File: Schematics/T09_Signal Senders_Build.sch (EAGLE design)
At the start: 27 parts, among them IC1 7805TV, IC2 ATMEGA328, SW1 , Y2 16MHz

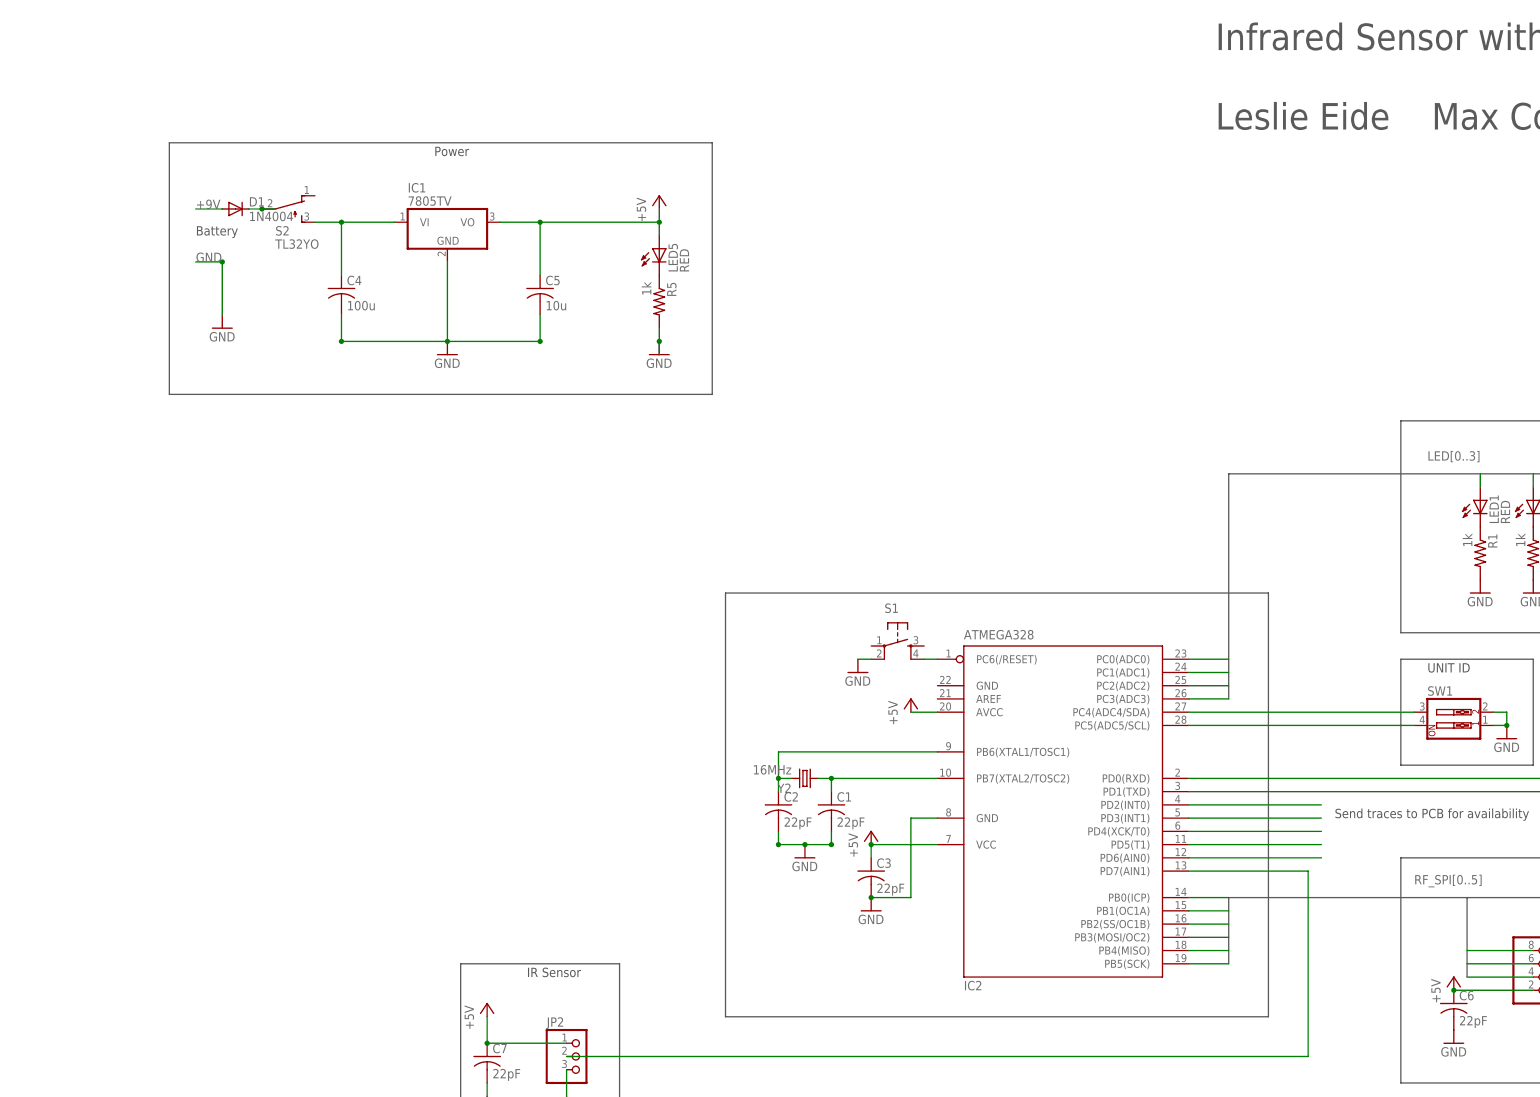
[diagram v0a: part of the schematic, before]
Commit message: Added 3.3V Rail. Can use panel mounted DC barrel.
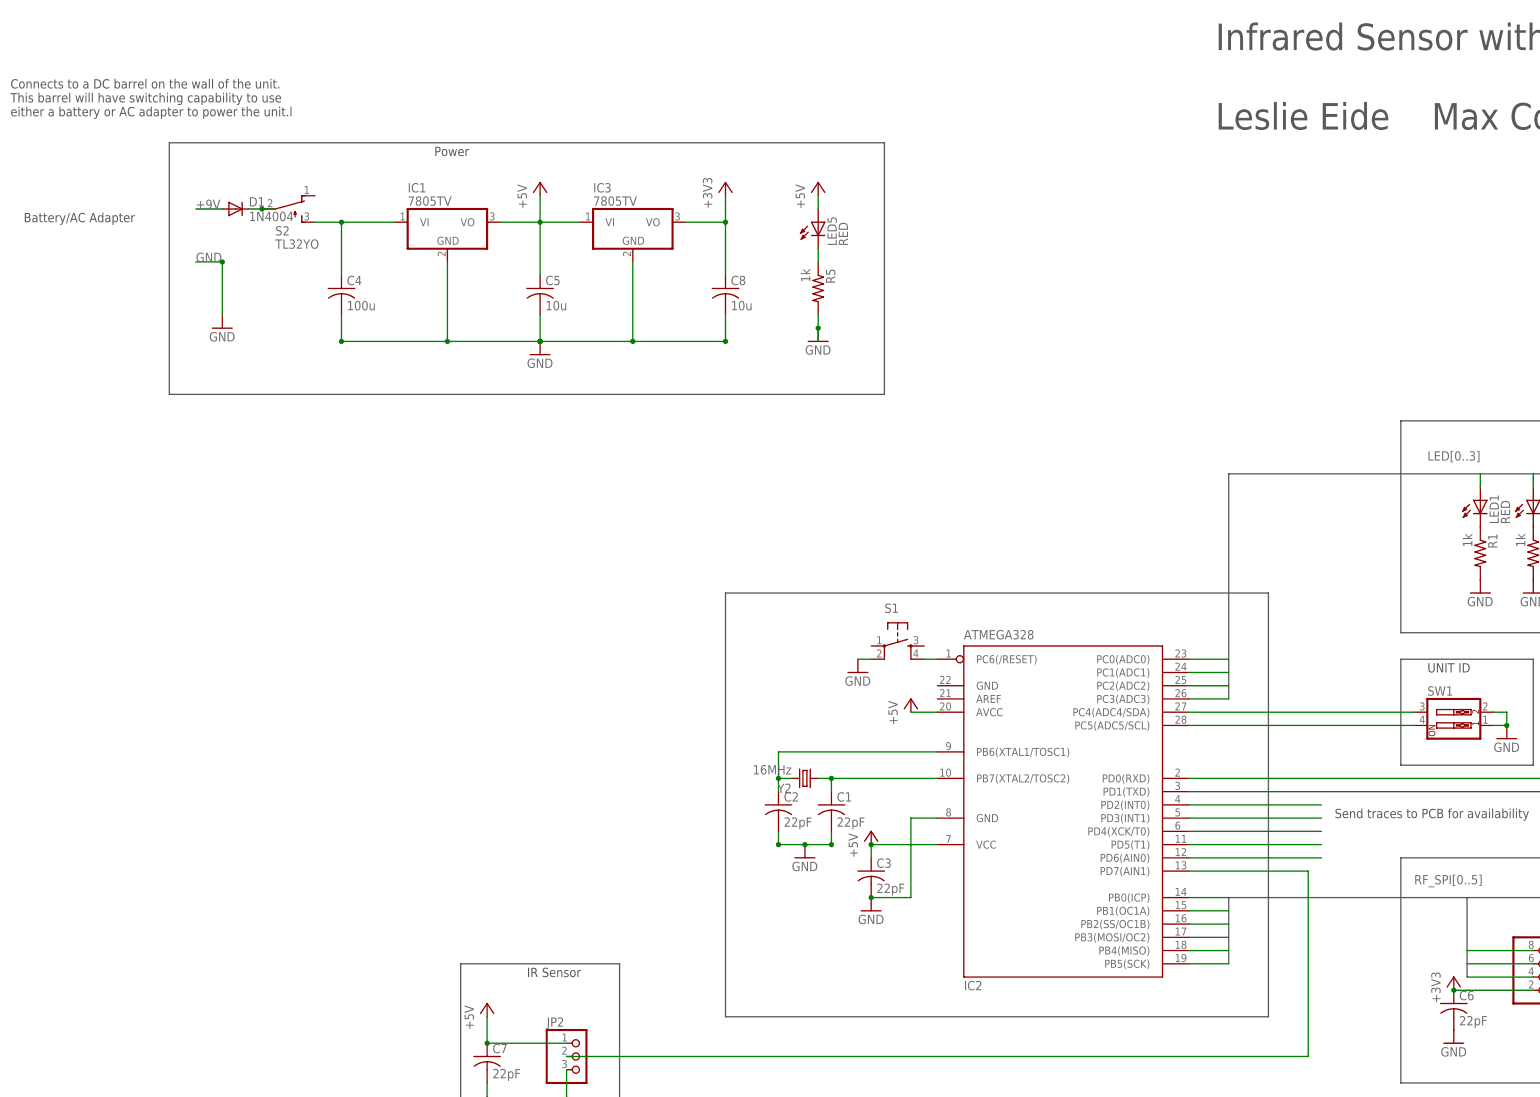
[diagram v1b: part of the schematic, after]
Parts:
- added C8: 10u, rcl:C-US025-025X050
- added IC3: 7805TV, linear:7805TV
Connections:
- new net +3V3: C6.1, C8.1, IC3.VO, JP1.2
- net +5V: now also IC3.VI; no longer C6.1, JP1.2
- net GND: now also C8.2, IC3.GND
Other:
- note added: "Battery/AC Adapter"
- note added: "Connects to a DC barrel on the wall of the unit. This barrel will have switching capability to use either a battery or AC adapter to power the unit.l"
- note removed: "Battery"
- moved on the sheet: LED5, R5

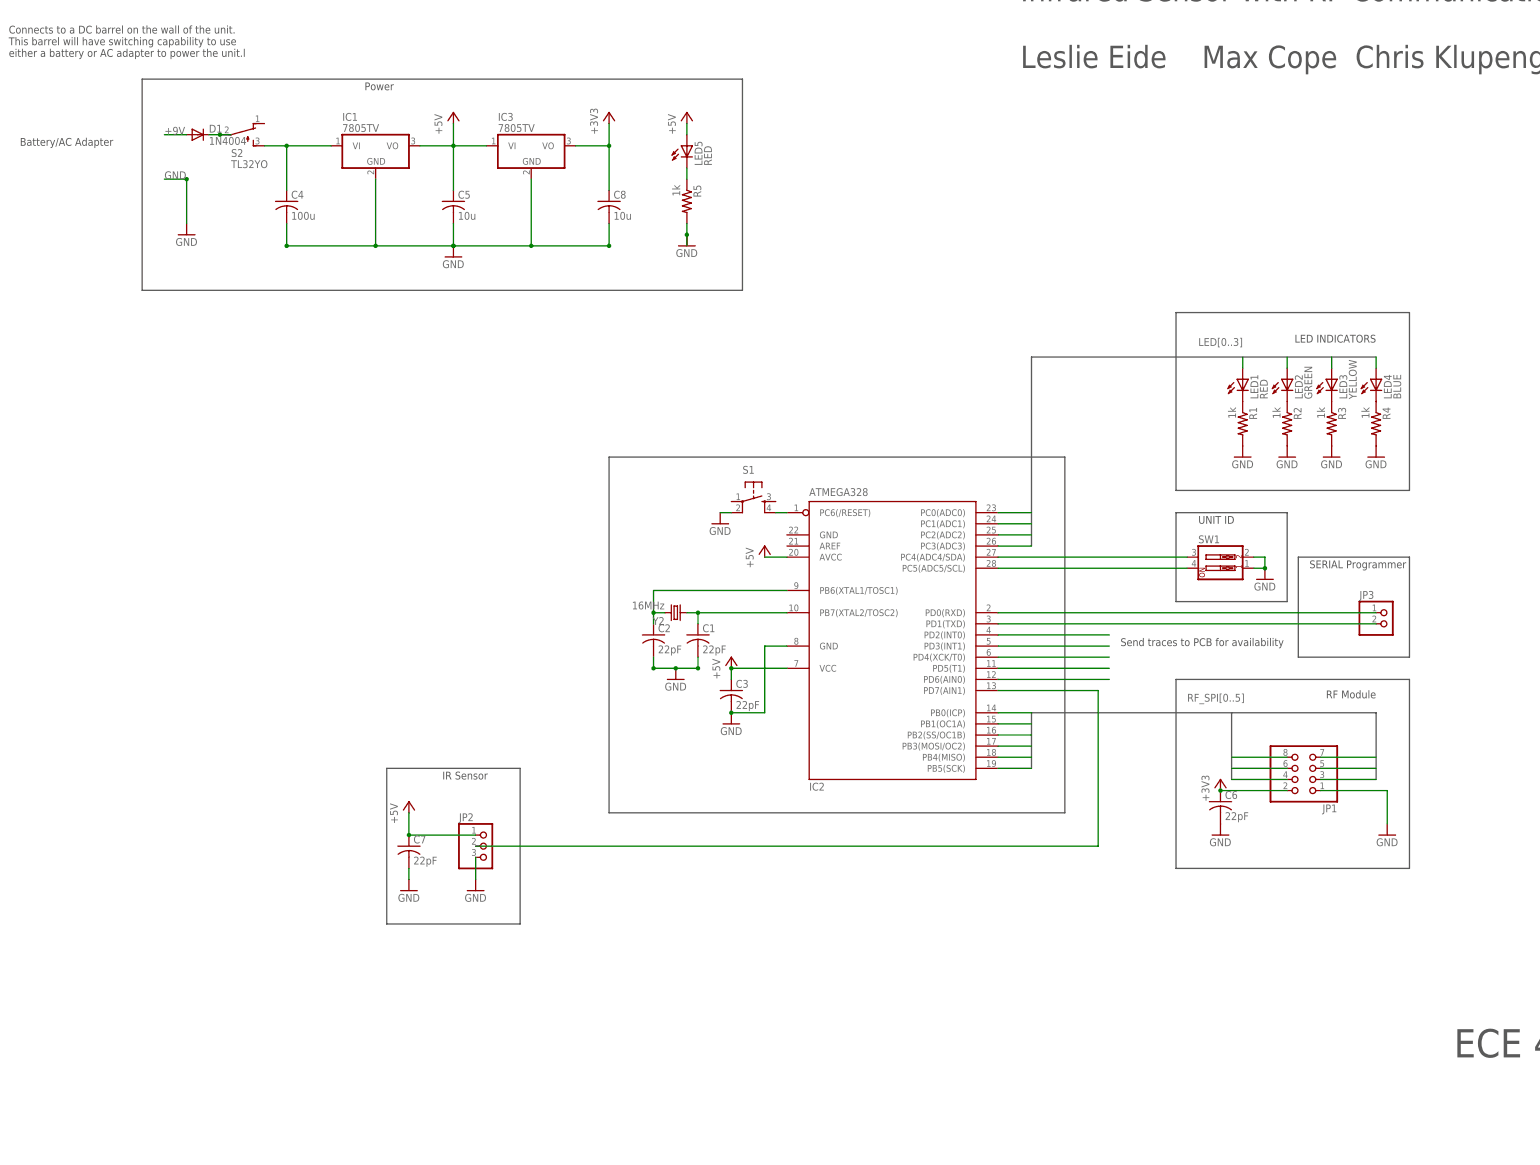
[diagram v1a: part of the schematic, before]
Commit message: Modified SPI section. Added DC barrel.
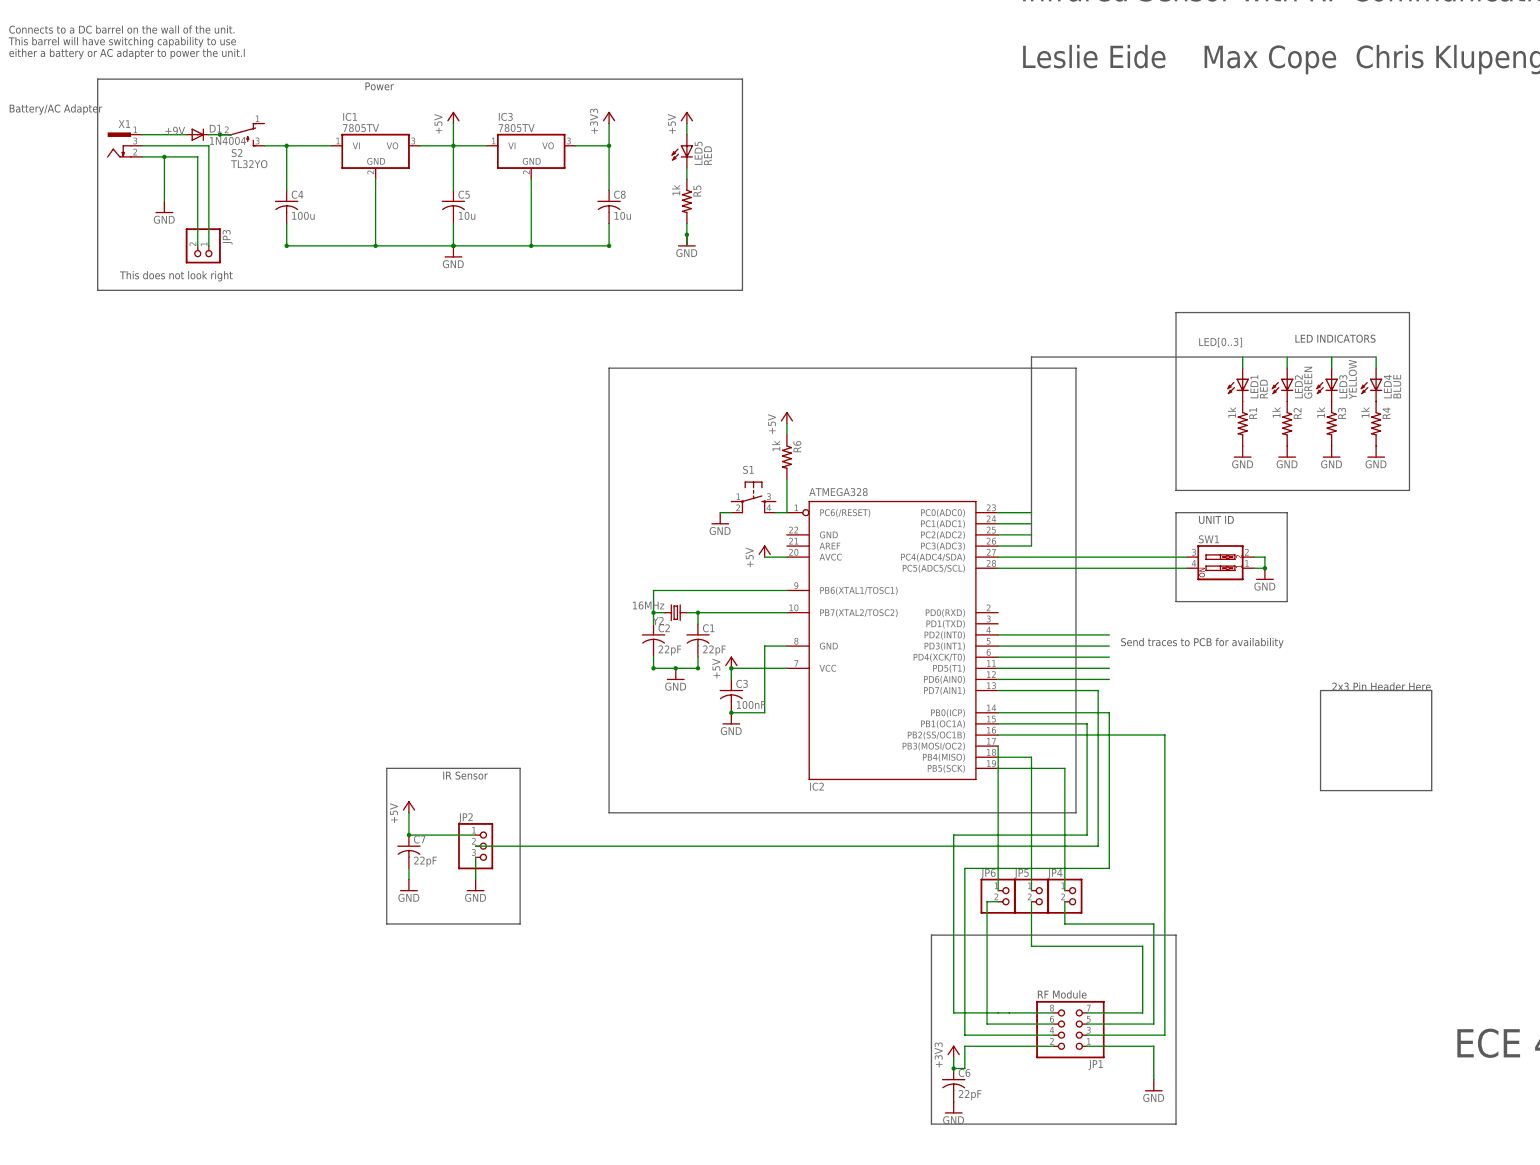
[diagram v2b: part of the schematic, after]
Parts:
- added JP4, JP5, JP6: (no value), pinhead:PINHD-1X2/90
- added R6: 1k, rcl:R-US_M0805
- added X1: (no value), con-conrad:733980-62
- C3: value 22pF -> 100nF
- JP3: value (none) -> (none); device pinhead:PINHD-1X2 -> pinhead:PINHD-1X2/90
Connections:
- removed net N$14: IC2.PD1(TXD), JP3.2
- net +5V: now also R6.1
- net +9V: now also X1.1
- net N$1: now also R6.2
- net N$13: now also X1.3; no longer IC2.PD0(RXD), JP3.1
- net RF_SPI0: now also IC2.PB2(SS/OC1B), JP1.4
- net RF_SPI1: now also JP1.8; no longer JP1.4
- net RF_SPI2: now also JP4.2; no longer IC2.PB2(SS/OC1B)
- net RF_SPI3: now also JP6.1, JP6.2
- net RF_SPI4: now also JP5.1, JP5.2
- net RF_SPI5: now also JP4.1; no longer JP1.8
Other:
- note added: "2x3 Pin Header Here"
- note added: "This does not look right"
- note removed: "SERIAL Programmer"
- moved on the sheet: C6, JP1, JP3
